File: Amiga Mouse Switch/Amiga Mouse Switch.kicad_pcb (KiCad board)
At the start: 2 copper layers, 82.5 x 40.6 mm, 21 parts, among them J1 Joystick 0, J2 Joystick 1, J3 CPC IDC, M1 Mounting, M2 Mounting, M3 Mounting, M4 Mounting, M5 Mounting, M6 Mounting

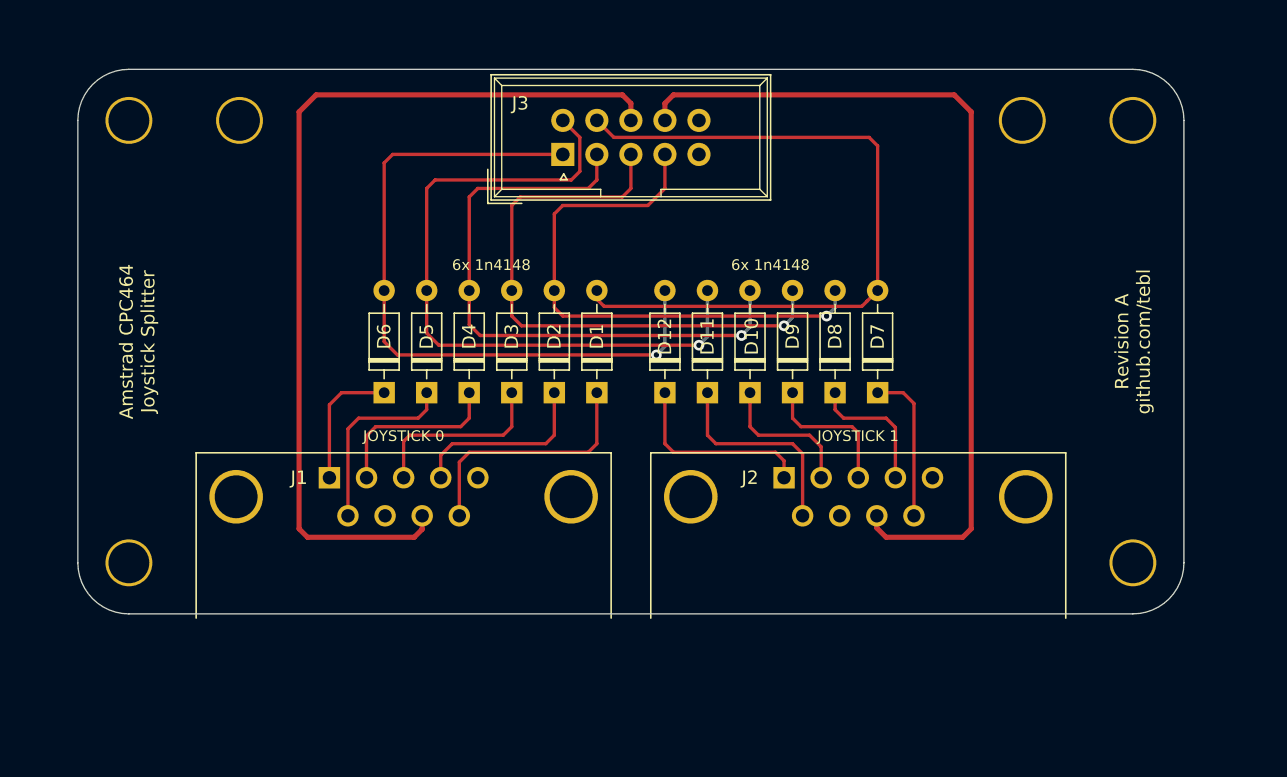
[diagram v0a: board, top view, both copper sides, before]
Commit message: Schematic done
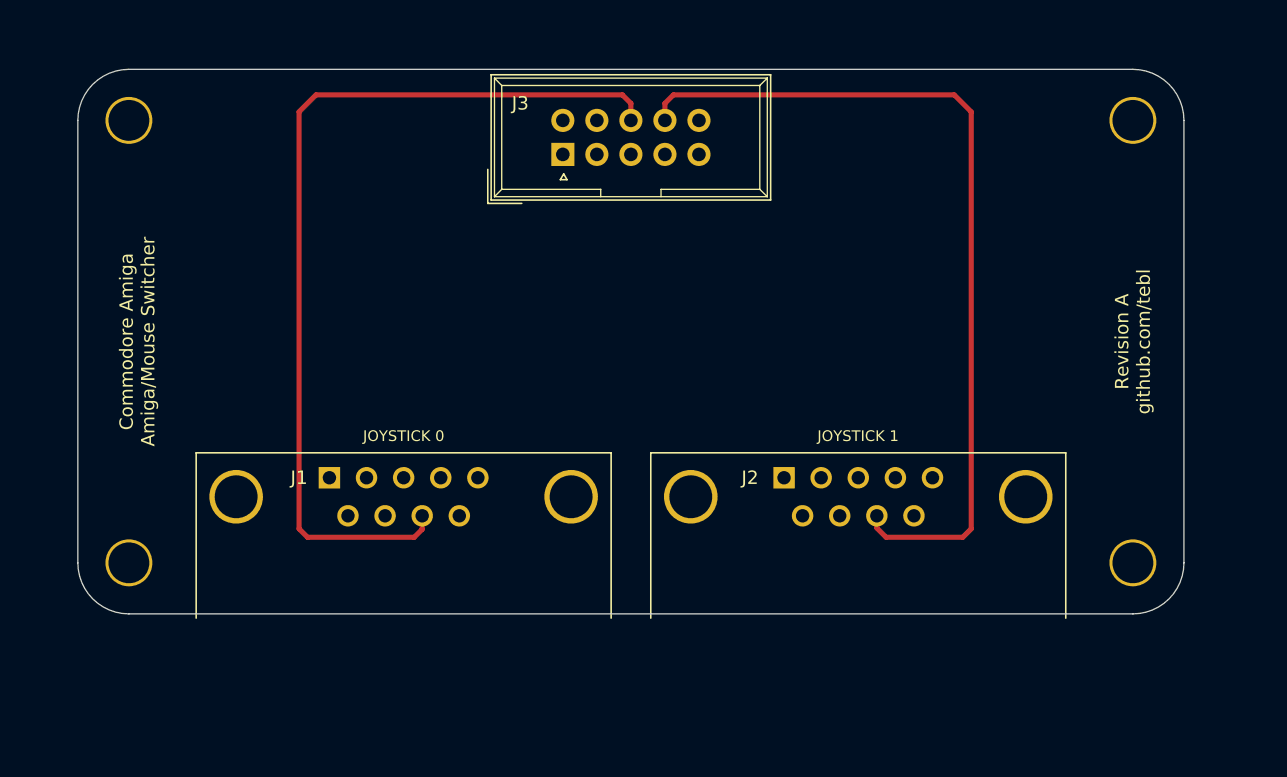
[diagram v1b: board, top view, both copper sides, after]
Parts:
- removed D1, D10, D11, D12, D2, D3, D4, D5, D6, D7, D8, D9: 1n4148, Diode_THT:D_DO-35_SOD27_P7.62mm_Horizontal
- removed M5, M6: Mounting, mounting:M3_pin
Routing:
- net /FIRE1: track 54.8 -> 0.00 mm
- net /UP: track 52.7 -> 0.00 mm, vias 1 -> 0
- net /FIRE2: track 52.1 -> 0.00 mm, vias 1 -> 0
- net /DOWN: track 45.8 -> 0.00 mm, vias 1 -> 0
- net /LEFT: track 43.7 -> 0.00 mm, vias 1 -> 0
- net /RIGHT: track 41.3 -> 0.00 mm, vias 1 -> 0
- net /P0_FIRE2: track 18.6 -> 0.00 mm
- net /P1_FIRE1: track 15.5 -> 0.00 mm
- net /P1_UP: track 14.5 -> 0.00 mm
- net /P0_FIRE1: track 14.2 -> 0.00 mm
- net /P0_RIGHT: track 14.0 -> 0.00 mm
- net /P0_LEFT: track 13.8 -> 0.00 mm
- net /P0_DOWN: track 13.2 -> 0.00 mm
- net /P1_FIRE2: track 11.4 -> 0.00 mm
- net /P1_DOWN: track 10.8 -> 0.00 mm
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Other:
- board text added: "Commodore Amiga Amiga/Mouse Switcher"
- board text removed: "6x 1n4148"
- board text removed: "Amstrad CPC464 Joystick Splitter"

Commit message: Layout done
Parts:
- added C1: 100nF, Capacitor_THT:C_Disc_D4.7mm_W2.5mm_P5.00mm, F.Cu at (148.0, 88.3)
- added C2: 100nF, Capacitor_THT:C_Disc_D4.7mm_W2.5mm_P5.00mm, F.Cu at (122.6, 88.3)
- added C3: 100nF, Capacitor_THT:C_Disc_D4.7mm_W2.5mm_P5.00mm, F.Cu at (107.3, 88.3)
- added D1: MOUSE, LED_THT:LED_D5.0mm, F.Cu at (177.2, 104.1)
- added D2: JOYSTICK, LED_THT:LED_D5.0mm, F.Cu at (102.2, 104.1)
- added JP1: AUTO_JOY, solder_bridge:bridge, F.Cu at (111.8, 75.6)
- added JP2: AUTO_MOUSE, solder_bridge:bridge, F.Cu at (120.0, 75.6)
- added R1: 10k, Resistor_THT:R_Axial_DIN0207_L6.3mm_D2.5mm_P10.16mm_Horizontal, F.Cu at (120.0, 83.2)
- added R2: 10k, Resistor_THT:R_Axial_DIN0207_L6.3mm_D2.5mm_P10.16mm_Horizontal, F.Cu at (120.0, 80.0)
- added R3: 220, Resistor_THT:R_Axial_DIN0207_L6.3mm_D2.5mm_P10.16mm_Horizontal, F.Cu at (103.5, 95.9)
- added R4: 220, Resistor_THT:R_Axial_DIN0207_L6.3mm_D2.5mm_P10.16mm_Horizontal, F.Cu at (100.3, 85.7)
- added SW1: JOY_SEL, switch_cutout:SW_PUSH_6mm, F.Cu at (177.2, 83.8)
- added SW2: MOUSE_SEL, switch_cutout:SW_PUSH_6mm, F.Cu at (177.2, 94.0)
- added U1: 74HCT4053, Package_DIP:DIP-16_W7.62mm_Socket_LongPads, F.Cu at (151.8, 94.6)
- added U2: 74HCT4053, Package_DIP:DIP-16_W7.62mm_Socket_LongPads, F.Cu at (126.4, 94.6)
- added U3: NE555, Package_DIP:DIP-8_W7.62mm_Socket_LongPads, F.Cu at (111.1, 94.6)
- J1: value Joystick 0 -> JOYSTICK
- J2: value Joystick 1 -> Mouse
- J3: value CPC IDC -> Amiga IDC
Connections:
- J1 pad 1: /P0_UP -> /UP
- J1 pad 2: /P0_DOWN -> /DOWN
- J1 pad 3: /P0_LEFT -> /LEFT
- J1 pad 4: /P0_RIGHT -> /RIGHT
- J1 pad 5: Net-(J1-Pad5) -> (no net)
- J1 pad 6: /P0_FIRE1 -> /FIRE1
- J1 pad 7: Net-(J1-Pad7) -> VCC
- J1 pad 8: /COM1 -> GND
- J1 pad 9: /P0_FIRE2 -> /FIRE2
- J2 pad 1: /P1_UP -> /V
- J2 pad 2: /P1_DOWN -> /H
- J2 pad 3: /P1_LEFT -> /VQ
- J2 pad 4: /P1_RIGHT -> /HQ
- J2 pad 5: Net-(J2-Pad5) -> (no net)
- J2 pad 6: /P1_FIRE1 -> /LMB
- J2 pad 7: Net-(J2-Pad7) -> VCC
- J2 pad 8: /COM2 -> GND
- J2 pad 9: /P1_FIRE2 -> /RMB
- J3 pad 1: /UP -> Net-(J3-Pad1)
- J3 pad 10: Net-(J3-Pad10) -> (no net)
- J3 pad 2: /DOWN -> Net-(J3-Pad2)
- J3 pad 3: /LEFT -> Net-(J3-Pad3)
- J3 pad 4: /RIGHT -> Net-(J3-Pad4)
- J3 pad 5: Net-(J3-Pad5) -> (no net)
- J3 pad 6: /FIRE2 -> Net-(J3-Pad6)
- J3 pad 7: /FIRE1 -> VCC
- J3 pad 8: /COM1 -> GND
- J3 pad 9: /COM2 -> Net-(J3-Pad9)
- M1 pad 1: Net-(M1-Pad1) -> (no net)
- M2 pad 1: Net-(M2-Pad1) -> (no net)
- M3 pad 1: Net-(M3-Pad1) -> (no net)
- M4 pad 1: Net-(M4-Pad1) -> (no net)
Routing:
- net VCC: track 0.00 -> 197.8 mm, vias 0 -> 3
- net PORT: track 0.00 -> 175.4 mm, vias 0 -> 6
- net Net-(JP1-Pad2): track 0.00 -> 132.3 mm, vias 0 -> 3
- net Net-(JP2-Pad2): track 0.00 -> 118.2 mm
- net Net-(D1-Pad2): track 0.00 -> 91.7 mm
- net /FIRE1: track 0.00 -> 69.5 mm, vias 0 -> 2
- net /COM1: track 68.6 -> 0.00 mm
- net /COM2: track 64.5 -> 0.00 mm
- net /LMB: track 0.00 -> 59.7 mm, vias 0 -> 6
- net /RIGHT: track 0.00 -> 46.6 mm
- net /DOWN: track 0.00 -> 42.2 mm, vias 0 -> 1
- net Net-(J3-Pad2): track 0.00 -> 37.6 mm, vias 0 -> 1
- net /RMB: track 0.00 -> 36.1 mm, vias 0 -> 1
- net /LEFT: track 0.00 -> 34.9 mm
- net /V: track 0.00 -> 28.7 mm, vias 0 -> 1
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- added copper zone on B.Cu, net GND
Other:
- board text added: "AUTO_JOY"
- board text added: "AUTO_MOUSE"
- board text added: "JOYSTICK"
- board text added: "MOUSE"
- board text removed: "JOYSTICK 0"
- board text removed: "JOYSTICK 1"

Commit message: Gerber export
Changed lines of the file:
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@@
     (descr "LED, diameter 5.0mm, 2 pins, http://cdn-reichelt.de/documents/datenblatt/A500/LL-504BC2E-009.pdf")
     (tags "LED diameter 5.0mm 2 pins")
-    (fp_text reference D1 (at 1.27 -3.96 90) (layer F.SilkS)
+    (fp_text reference D1 (at 1.27 5.08 90) (layer F.SilkS)
       (effects (font (size 1 1) (thickness 0.15)))
     )
@@
     (descr "LED, diameter 5.0mm, 2 pins, http://cdn-reichelt.de/documents/datenblatt/A500/LL-504BC2E-009.pdf")
     (tags "LED diameter 5.0mm 2 pins")
-    (fp_text reference D2 (at 1.27 -3.96 90) (layer F.SilkS)
+    (fp_text reference D2 (at 1.27 -4.445 90) (layer F.SilkS)
       (effects (font (size 1 1) (thickness 0.15)))
     )
@@
     )
   )
-  (gr_text AUTO_MOUSE (at 119.0625 77.7875) (layer F.SilkS)
+  (gr_text AUTO_MOUSE (at 119.0625 73.025) (layer F.SilkS)
     (effects (font (size 0.8 0.8) (thickness 0.1)))
   )
-  (gr_text AUTO_JOY (at 110.8075 77.7875) (layer F.SilkS)
+  (gr_text AUTO_JOY (at 110.8075 73.025) (layer F.SilkS)
     (effects (font (size 0.8 0.8) (thickness 0.1)))
   )

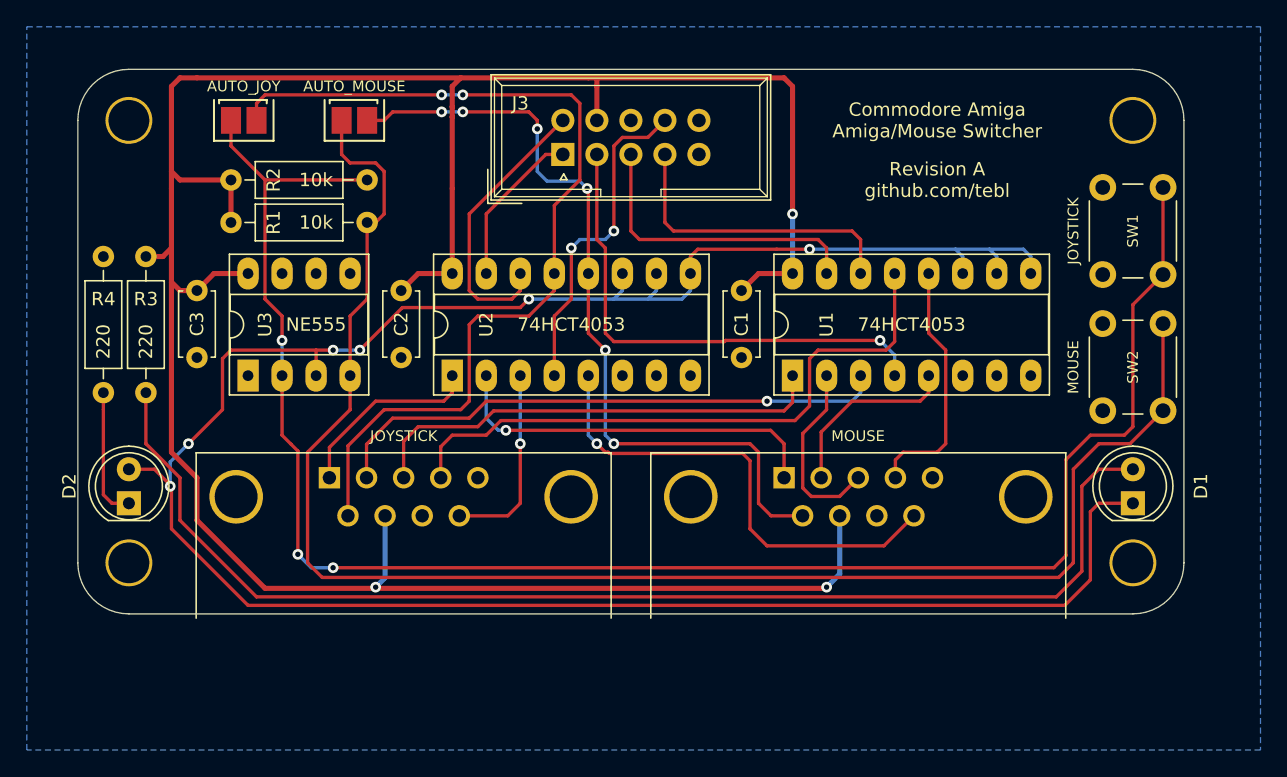
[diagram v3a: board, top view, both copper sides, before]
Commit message: Added diode for lines that have pull-ups onboard
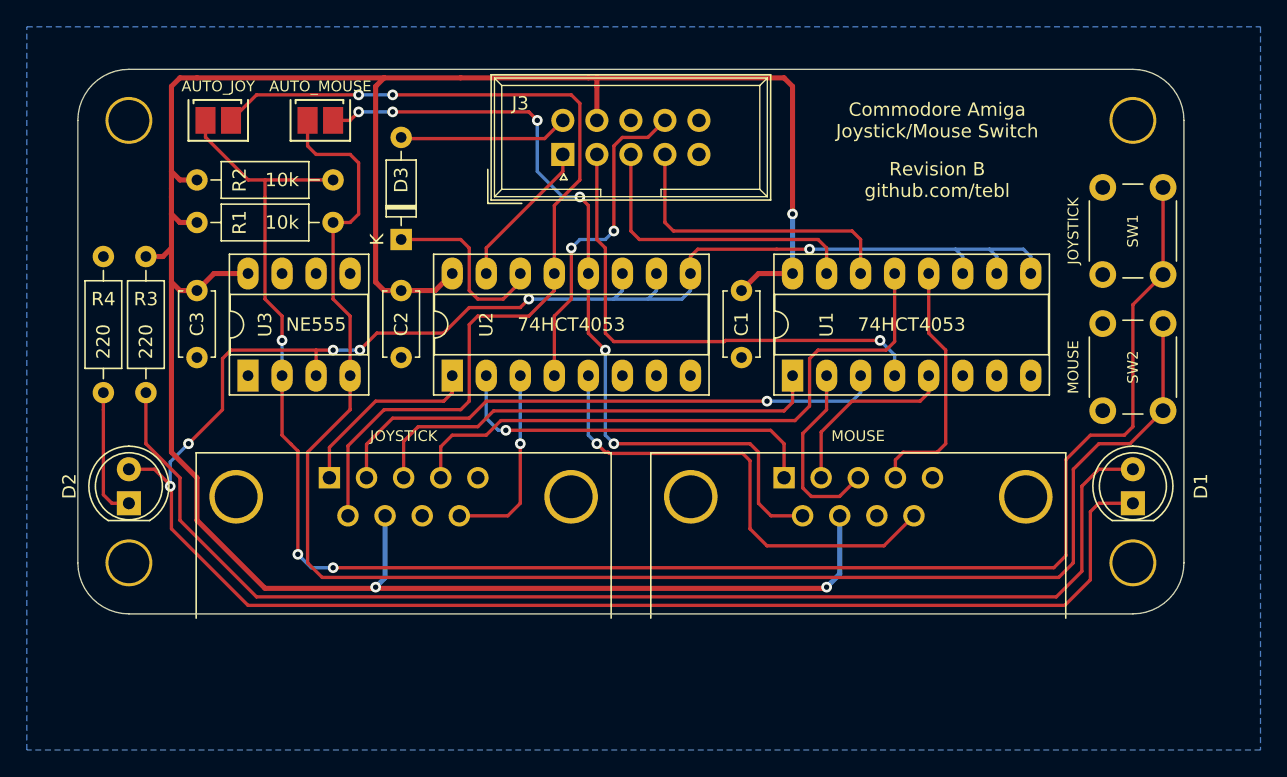
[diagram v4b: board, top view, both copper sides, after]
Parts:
- added D3: 1n4148, Diode_THT:D_DO-35_SOD27_P7.62mm_Horizontal, F.Cu at (122.6, 84.5)
- moved JP2 2.54 mm to (117.5, 75.6)
- moved R1 2.54 mm to (117.5, 83.2)
- moved R2 2.54 mm to (117.5, 80.0)
- moved JP1 1.91 mm to (109.9, 75.6)
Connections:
- J3 pad 6: Net-(J3-Pad6) -> Net-(D3-Pad2)
- U2 pad 14: Net-(J3-Pad6) -> Net-(D3-Pad1)
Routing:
- net Net-(J3-Pad6): track 21.2 -> 0.00 mm
- net Net-(D3-Pad1): track 0.00 -> 13.8 mm
- net Net-(D3-Pad2): track 0.00 -> 12.7 mm
- net /LMB: track 59.7 -> 61.6 mm
- net Net-(JP2-Pad2): track 118.2 -> 119.5 mm
- net /FIRE1: track 69.5 -> 70.6 mm
- net Net-(JP1-Pad2): track 132.3 -> 131.3 mm
- net VCC: track 197.8 -> 197.0 mm
- net Net-(J3-Pad1): track 12.0 -> 11.3 mm
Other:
- board text added: "Commodore Amiga Joystick/Mouse Switch"
- board text added: "Revision B github.com/tebl"
- board text removed: "Commodore Amiga Amiga/Mouse Switcher"
- board text removed: "Revision A github.com/tebl"

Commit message: Fixed RMB
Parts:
- added D4: 1n4148, Diode_THT:D_DO-35_SOD27_P7.62mm_Horizontal, F.Cu at (169.5, 98.0)
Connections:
- J3 pad 9: Net-(J3-Pad9) -> /FIRE2
- U2 pad 3: /FIRE2 -> GND
- U2 pad 4: Net-(J3-Pad9) -> (no net)
- U2 pad 5: /RMB -> GND
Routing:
- net /FIRE2: track 14.5 -> 83.2 mm, vias 1 -> 5
- net Net-(J3-Pad9): track 24.7 -> 0.00 mm, vias 2 -> 0
- net /RMB: track 36.1 -> 14.8 mm, vias 1 -> 0
- net Net-(J3-Pad1): track 11.3 -> 13.9 mm

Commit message: Added README
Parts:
- R3, R4: value 220 -> 330

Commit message: Tweaks for RMB (untested)
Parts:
- removed D4: 1n4148, Diode_THT:D_DO-35_SOD27_P7.62mm_Horizontal
- added JP3: EN_SCROLL, solder_bridge:bridge, F.Cu at (168.3, 83.2)
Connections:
- J1 pad 9: /FIRE2 -> (no net)
- J2 pad 5: (no net) -> SCROLL
- J2 pad 9: /RMB -> RMB
- J3 pad 5: (no net) -> Net-(J3-Pad5)
- J3 pad 9: /FIRE2 -> RMB
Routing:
- net RMB: track 0.00 -> 93.4 mm, vias 0 -> 4
- net /FIRE2: track 83.2 -> 0.00 mm, vias 5 -> 0
- net Net-(J3-Pad5): track 0.00 -> 25.9 mm
- net SCROLL: track 0.00 -> 24.5 mm
- net /RMB: track 14.8 -> 0.00 mm
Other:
- board text added: "EN_SCROLL"
- board text added: "Revision C github.com/tebl"
- board text removed: "Revision B github.com/tebl"
